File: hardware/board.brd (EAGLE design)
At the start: 53 x 30 mm, 45 parts, among them IC1 0915BM15A0001, J1 U.FL, U3 BLE113-A, X1 CTS_32X25_SMD, X3 MINI-USB-UX60-MB-5ST

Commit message: Update value of bias resistor
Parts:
- R3: value 58kOhm -> 56kOhm ± 1%
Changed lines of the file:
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@@
 <layer number="27" name="tValues" color="7" fill="1" visible="no" active="yes"/>
 <layer number="28" name="bValues" color="7" fill="1" visible="no" active="yes"/>
-<layer number="29" name="tStop" color="7" fill="3" visible="no" active="yes"/>
+<layer number="29" name="tStop" color="7" fill="3" visible="yes" active="yes"/>
 <layer number="30" name="bStop" color="7" fill="6" visible="no" active="yes"/>
 <layer number="31" name="tCream" color="7" fill="4" visible="no" active="yes"/>
@@
 <attribute name="VALUE" x="3.175" y="21.205" size="1.27" layer="27" rot="R180"/>
 </element>
-<element name="R3" library="rcl" package="R0402" value="58kOhm" x="21.3" y="3.5" smashed="yes" rot="R90">
+<element name="R3" library="rcl" package="R0402" value="56kOhm ± 1%" x="21.3" y="3.5" smashed="yes" rot="R90">
 <attribute name="VALUE" x="23.205" y="2.865" size="1.27" layer="27" rot="R90"/>
 </element>

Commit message: Update crystal value and part number
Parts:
- X1: value CTS_32X25_SMD -> 26MHz 10pF 10ppm -20C +70C
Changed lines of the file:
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@@
 <attribute name="VALUE" x="38.57" y="12.825" size="1.016" layer="27" rot="SR0"/>
 </element>
-<element name="X1" library="cts_crystal" package="CTS_32X25" value="CTS_32X25_SMD" x="17.985" y="14.645" smashed="yes">
+<element name="X1" library="cts_crystal" package="CTS_32X25" value="26MHz 10pF 10ppm -20C +70C" x="17.985" y="14.645" smashed="yes">
 <attribute name="VALUE" x="16.285" y="12.545" size="0.75" layer="27"/>
 </element>

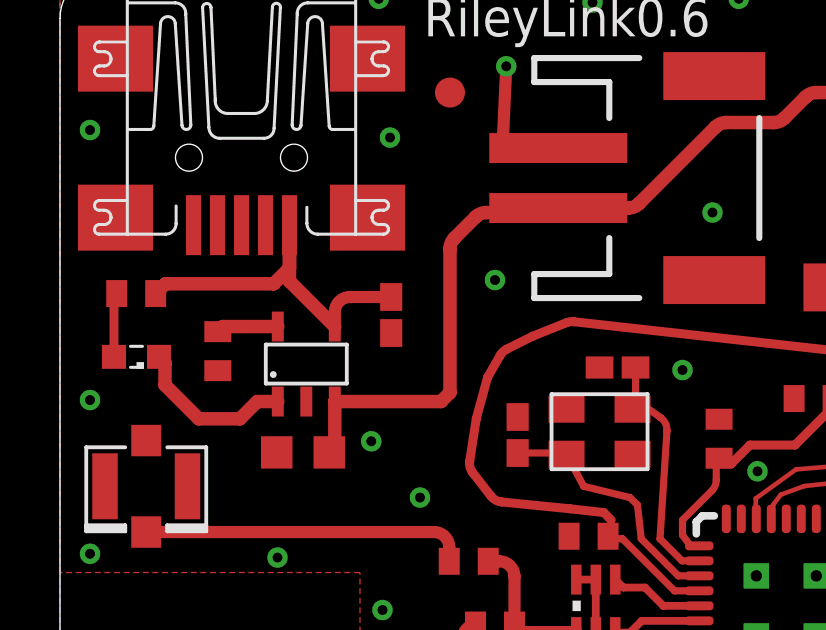
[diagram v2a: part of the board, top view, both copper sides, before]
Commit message: Add colors to leds, and switch 4.7uF cap from 0402 to 0603 package
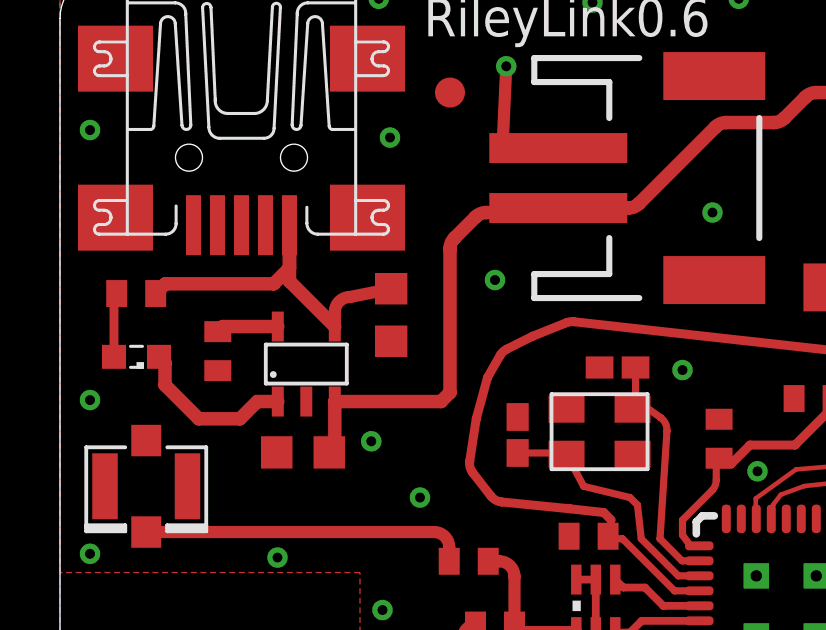
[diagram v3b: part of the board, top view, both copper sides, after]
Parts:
- C2: device rcl:C0402K -> rcl:C0603K
- LED1: value (none) -> red
- LED2, LED5: value (none) -> blue
- LED3, LED4: value (none) -> green
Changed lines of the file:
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@@
 <attribute name="VALUE" x="18.255" y="13.115" size="1.27" layer="27" rot="R180"/>
 </element>
-<element name="C2" library="rcl" package="C0402K" value="4.7uF" x="11.04" y="18.585" smashed="yes" rot="R270">
+<element name="C2" library="rcl" package="C0603K" value="4.7uF" x="11.04" y="18.585" smashed="yes" rot="R270">
 <attribute name="VALUE" x="9.59" y="19.085" size="1.016" layer="27" rot="R270"/>
 </element>
@@
 <attribute name="VALUE" x="26.9524" y="16.8466" size="2.0828" layer="27" ratio="10" rot="SR0"/>
 </element>
-<element name="LED1" library="led" package="SML0603" value="" x="2.55" y="17.19" smashed="yes" rot="R180">
+<element name="LED1" library="led" package="SML0603" value="red" x="2.55" y="17.19" smashed="yes" rot="R180">
 <attribute name="VALUE" x="3.55" y="19.19" size="1.27" layer="27" rot="R180"/>
 </element>
-<element name="LED2" library="led" package="SML0603" value="" x="51.65" y="19.05" smashed="yes" rot="R90">
+<element name="LED2" library="led" package="SML0603" value="blue" x="51.65" y="19.05" smashed="yes" rot="R90">
 <attribute name="VALUE" x="53.65" y="18.05" size="1.27" layer="27" rot="R90"/>
 </element>
-<element name="LED3" library="led" package="SML0603" value="" x="51.65" y="22.51" smashed="yes" rot="R90">
+<element name="LED3" library="led" package="SML0603" value="green" x="51.65" y="22.51" smashed="yes" rot="R90">
 <attribute name="VALUE" x="53.65" y="21.51" size="1.27" layer="27" rot="R90"/>
 </element>
-<element name="LED4" library="led" package="SML0603" value="" x="35.25" y="13.25" smashed="yes" rot="R270">
+<element name="LED4" library="led" package="SML0603" value="green" x="35.25" y="13.25" smashed="yes" rot="R270">
 <attribute name="VALUE" x="33.25" y="14.25" size="1.27" layer="27" rot="R270"/>
 </element>
-<element name="LED5" library="led" package="SML0603" value="" x="33.75" y="13.25" smashed="yes" rot="R270">
+<element name="LED5" library="led" package="SML0603" value="blue" x="33.75" y="13.25" smashed="yes" rot="R270">
 <attribute name="VALUE" x="31.75" y="14.25" size="1.27" layer="27" rot="R270"/>
 </element>
@@
 <wire x1="7.125" y1="19.625" x2="3.515" y2="19.625" width="0.45" layer="1"/>
 <wire x1="3.515" y1="19.625" x2="3.19" y2="19.3" width="0.45" layer="1"/>
-<wire x1="11.04" y1="19.185" x2="9.668" y2="19.185" width="0.4064" layer="1"/>
+<wire x1="11.04" y1="19.46" x2="9.668" y2="19.185" width="0.4064" layer="1"/>
 <wire x1="9.668" y1="19.185" x2="9.16" y2="18.677" width="0.4064" layer="1" curve="90"/>
 <wire x1="9.16" y1="18.677" x2="9.16" y2="18.2" width="0.4064" layer="1"/>

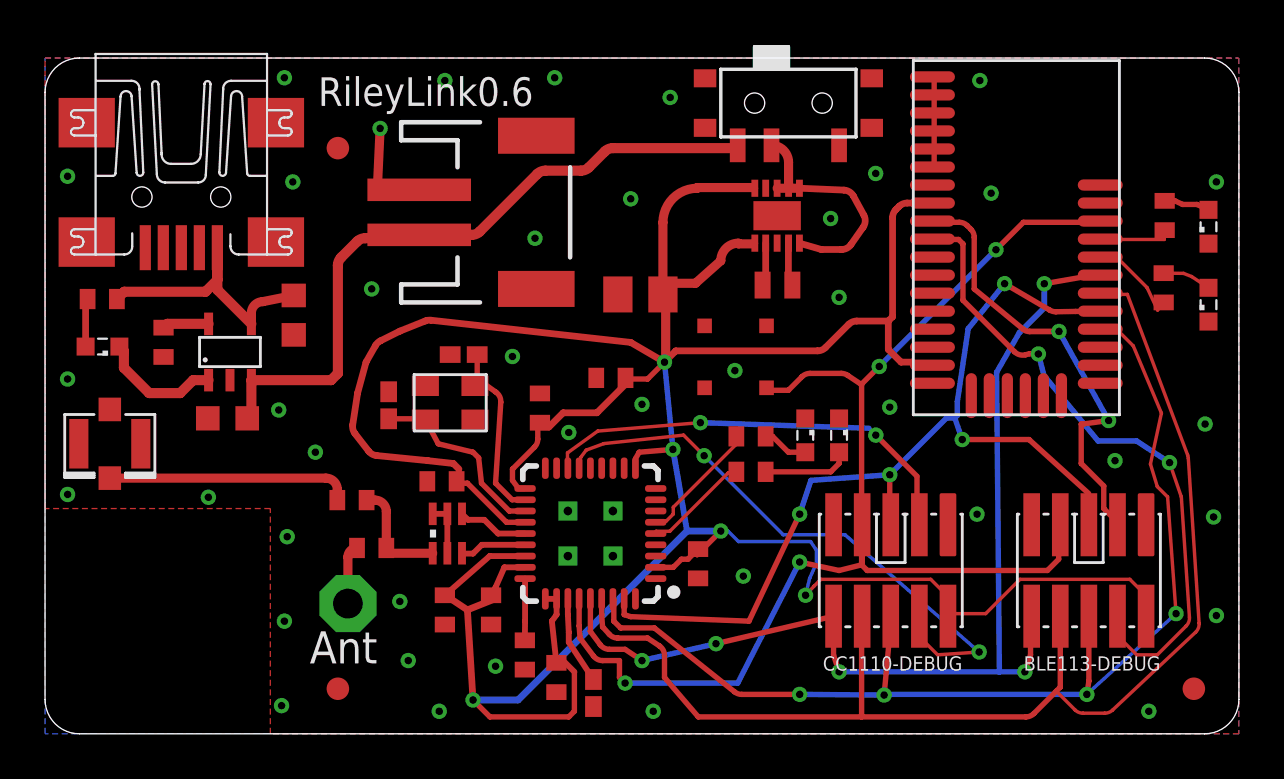
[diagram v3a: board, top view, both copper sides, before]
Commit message: Update C11 to 0805
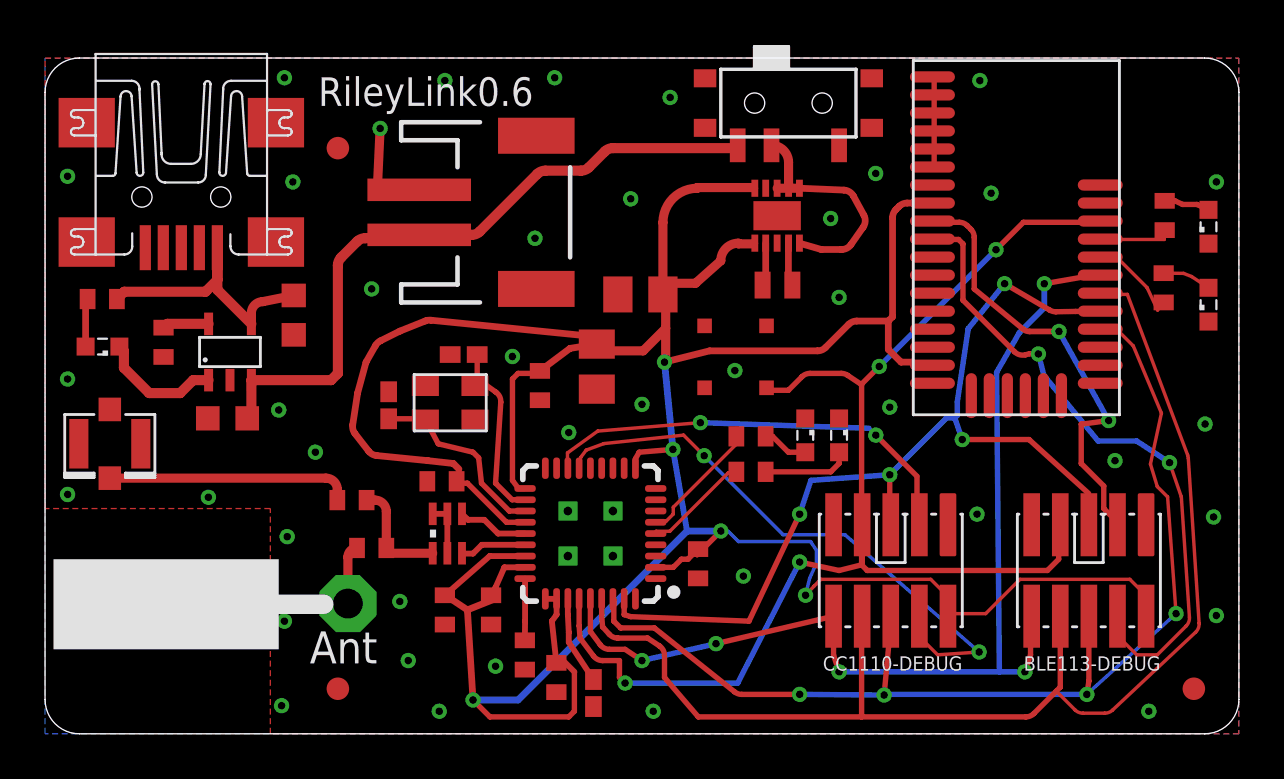
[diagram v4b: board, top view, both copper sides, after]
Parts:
- C11: device rcl:C0402 -> rcl:C0805K
- moved C12 1.00 mm to (22.0, 15.5), turned to 270 degrees
- moved C11 0.80 mm to (24.5, 16.3), turned to 270 degrees
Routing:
- net VDD: track 152.6 -> 151.7 mm
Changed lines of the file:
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@@
 <layer number="27" name="tValues" color="7" fill="1" visible="no" active="yes"/>
 <layer number="28" name="bValues" color="7" fill="1" visible="no" active="yes"/>
-<layer number="29" name="tStop" color="7" fill="3" visible="yes" active="yes"/>
+<layer number="29" name="tStop" color="7" fill="3" visible="no" active="yes"/>
 <layer number="30" name="bStop" color="7" fill="6" visible="no" active="yes"/>
 <layer number="31" name="tCream" color="7" fill="4" visible="no" active="yes"/>
@@
 <text x="12.125" y="27.875" size="1.27" layer="25">RileyLink0.6</text>
 <text x="11.75" y="3.125" size="1.4224" layer="25">Ant</text>
+<wire x1="12.375" y1="5.75" x2="10.375" y2="5.75" width="0.8636" layer="112"/>
+<rectangle x1="0.375" y1="3.75" x2="10.375" y2="7.75" layer="112"/>
 </plain>
 <attributes>
@@
 <attribute name="VALUE" x="17.895" y="6.135" size="1.27" layer="27" rot="R270"/>
 </element>
-<element name="C11" library="rcl" package="C0402" value="100uF" x="25.12" y="15.8" smashed="yes" rot="R180">
-<attribute name="VALUE" x="25.755" y="17.705" size="1.27" layer="27" rot="R180"/>
-</element>
-<element name="C12" library="rcl" package="C0402" value="100nF" x="21.97" y="14.46" smashed="yes" rot="R90">
-<attribute name="VALUE" x="23.875" y="13.825" size="1.27" layer="27" rot="R90"/>
+<element name="C11" library="rcl" package="C0805K" value="100uF" x="24.495" y="16.3" smashed="yes" rot="R270">
+<attribute name="VALUE" x="22.59" y="16.935" size="1.27" layer="27" rot="R270"/>
+</element>
+<element name="C12" library="rcl" package="C0402" value="100nF" x="21.97" y="15.46" smashed="yes" rot="R270">
+<attribute name="VALUE" x="20.065" y="16.095" size="1.27" layer="27" rot="R270"/>
 </element>
 <element name="C13" library="rcl" package="C0402" value="100nF" x="17.62" y="11.21" smashed="yes" rot="R180">
@@
 <wire x1="19.75" y1="0.75" x2="19" y2="1.5" width="0.24" layer="1"/>
 <via x="27.5" y="16.5" extent="1-16" drill="0.3302"/>
-<wire x1="27.5" y1="16.5" x2="27.875" y2="12.625" width="0.24" layer="16"/>
-<wire x1="27.5" y1="16.5" x2="26.75" y2="15.75" width="0.24" layer="1"/>
-<wire x1="26.75" y1="15.75" x2="25.7556" y2="15.75" width="0.24" layer="1"/>
+<wire x1="27.5" y1="16.5" x2="27.875" y2="12.625" width="0.3" layer="16"/>
 <via x="27.875" y="12.625" extent="1-16" drill="0.3302"/>
-<wire x1="25.7556" y1="15.75" x2="25.75" y2="15.75" width="0.24" layer="1"/>
 <wire x1="26.21" y1="11.79" x2="26.21" y2="12.21" width="0.24" layer="1"/>
 <wire x1="26.21" y1="12.21" x2="26.375" y2="12.5" width="0.24" layer="1"/>
@@
 <wire x1="38.5572" y1="16.4592" x2="39.3192" y2="16.4592" width="0.1524" layer="1"/>
 <wire x1="39.3192" y1="16.4592" x2="39.395" y2="16.3625" width="0.1524" layer="1"/>
-<wire x1="25.7556" y1="15.8496" x2="25.77" y2="15.8" width="0.1524" layer="1"/>
-<wire x1="25.7556" y1="15.8496" x2="25.7556" y2="15.75" width="0.1524" layer="1"/>
 <wire x1="40.0812" y1="6.096" x2="40.0812" y2="5.334" width="0.1524" layer="1"/>
 <wire x1="39.3192" y1="6.858" x2="40.0812" y2="6.096" width="0.1524" layer="1"/>
@@
 <wire x1="21.31" y1="10.89" x2="21.015" y2="10.89" width="0.24" layer="1"/>
 <wire x1="21.015" y1="10.89" x2="20.75" y2="11.25" width="0.24" layer="1"/>
-<wire x1="20.75" y1="11.25" x2="20.75" y2="11.75" width="0.24" layer="1"/>
-<wire x1="20.75" y1="11.75" x2="21.726209375" y2="12.726209375" width="0.24" layer="1"/>
-<wire x1="21.726209375" y1="12.726209375" x2="21.875" y2="13.085421875" width="0.24" layer="1" curve="45.000352"/>
-<wire x1="21.875" y1="13.085421875" x2="21.875" y2="13.625" width="0.24" layer="1"/>
-<wire x1="21.875" y1="13.625" x2="21.875" y2="13.715" width="0.24" layer="1"/>
-<wire x1="21.875" y1="13.715" x2="21.97" y2="13.81" width="0.24" layer="1"/>
 <wire x1="21.31" y1="9.39" x2="20.485" y2="9.39" width="0.24" layer="1"/>
 <wire x1="20.485" y1="9.39" x2="18.75" y2="11.125" width="0.24" layer="1"/>
@@
 <wire x1="15.75" y1="17.875" x2="16.88178125" y2="18.3277125" width="0.3" layer="1"/>
 <wire x1="16.88178125" y1="18.3277125" x2="17.126546875" y2="18.360940625" width="0.3" layer="1" curve="-28.141614"/>
-<wire x1="17.126546875" y1="18.360940625" x2="26" y2="17.375" width="0.3" layer="1"/>
 <wire x1="18.355" y1="11.125" x2="18.355" y2="11.23" width="0.24" layer="1"/>
 <wire x1="18.355" y1="11.23" x2="18.375" y2="11.25" width="0.24" layer="1"/>
-<wire x1="28" y1="17" x2="27.5" y2="16.5" width="0.3" layer="1"/>
 <wire x1="37.4356" y1="18.324" x2="36.034421875" y2="18.324" width="0.3" layer="1"/>
 <wire x1="36.034421875" y1="18.324" x2="35.675209375" y2="18.175209375" width="0.3" layer="1" curve="45.000249"/>
 <wire x1="35.675209375" y1="18.175209375" x2="34.648790625" y2="17.148790625" width="0.3" layer="1"/>
 <wire x1="34.648790625" y1="17.148790625" x2="34.289578125" y2="17" width="0.3" layer="1" curve="-45.000352"/>
-<wire x1="34.289578125" y1="17" x2="28" y2="17" width="0.3" layer="1"/>
+<wire x1="34.289578125" y1="17" x2="29.5" y2="17" width="0.3" layer="1"/>
 <wire x1="37.4356" y1="18.324" x2="37.4356" y2="17.0644" width="0.3" layer="1"/>
 <wire x1="37.4356" y1="17.0644" x2="38" y2="16.5" width="0.3" layer="1"/>
@@
 <wire x1="37.625" y1="22.914578125" x2="37.625" y2="18.5134" width="0.3" layer="1"/>
 <wire x1="37.625" y1="18.5134" x2="37.4356" y2="18.324" width="0.3" layer="1"/>
-<wire x1="26" y1="17.375" x2="27.5" y2="16.5" width="0.3" layer="1"/>
-<wire x1="21.875" y1="13.625" x2="22.375" y2="13.625" width="0.3" layer="1"/>
-<wire x1="22.375" y1="13.625" x2="23" y2="14.25" width="0.3" layer="1"/>
-<wire x1="23" y1="14.25" x2="24.5" y2="14.25" width="0.3" layer="1"/>
-<wire x1="24.5" y1="14.25" x2="25.875" y2="15.625" width="0.3" layer="1"/>
-<wire x1="25.7556" y1="15.75" x2="25.7556" y2="15.7444" width="0.3" layer="1"/>
-<wire x1="25.7556" y1="15.7444" x2="25.875" y2="15.625" width="0.3" layer="1"/>
 <wire x1="28.954" y1="24.2192" x2="27.43" y2="22.6952" width="0.4064" layer="1" curve="90"/>
 <wire x1="27.43" y1="22.6952" x2="27.43" y2="19.505" width="0.4064" layer="1"/>
@@
 <wire x1="27.925" y1="20" x2="27.43" y2="19.505" width="0.4064" layer="1" curve="90"/>
 <wire x1="27.43" y1="19.505" x2="27.552578125" y2="19.382421875" width="0.4064" layer="1" curve="-90"/>
-<wire x1="27.552578125" y1="19.382421875" x2="27.552578125" y2="16.4567" width="0.4064" layer="1"/>
+<wire x1="27.552578125" y1="19.382421875" x2="27.552578125" y2="18" width="0.4064" layer="1"/>
+<wire x1="27.552578125" y1="18" x2="27.552578125" y2="16.4567" width="0.4064" layer="1"/>
 <wire x1="31.5094" y1="24.2192" x2="31.375" y2="24.2192" width="0.3048" layer="1"/>
 <wire x1="31.375" y1="24.2192" x2="31.375" y2="24.25" width="0.3048" layer="1"/>
@@
 <wire x1="31.375" y1="21.75" x2="30.7808" y2="21.75" width="0.4064" layer="1"/>
 <wire x1="30.7808" y1="21.75" x2="30.7808" y2="21.7808" width="0.4064" layer="1"/>
-<wire x1="27.5" y1="16.5" x2="27.552578125" y2="16.4567" width="0" layer="19" extent="1-1"/>
+<wire x1="20.75" y1="11.25" x2="20.75" y2="15.75" width="0.24" layer="1"/>
+<wire x1="20.75" y1="15.75" x2="21" y2="16" width="0.24" layer="1"/>
+<wire x1="21" y1="16" x2="21.86" y2="16" width="0.24" layer="1"/>
+<wire x1="21.97" y1="16.11" x2="23.305" y2="17.11" width="0.3" layer="1"/>
+<wire x1="23.305" y1="17.11" x2="24.495" y2="17.3" width="0.3" layer="1"/>
+<wire x1="24.795" y1="17" x2="24.495" y2="17.3" width="0.3" layer="1"/>
+<wire x1="24.4874875" y1="17.625" x2="17.126546875" y2="18.360940625" width="0.3" layer="1"/>
+<wire x1="24.495" y1="17.3" x2="24.495" y2="17.6174875" width="0.3" layer="1"/>
+<wire x1="24.495" y1="17.6174875" x2="24.4874875" y2="17.625" width="0.3" layer="1"/>
+<wire x1="29.5" y1="17" x2="27.5" y2="16.5" width="0.3" layer="1"/>
+<wire x1="27.552578125" y1="16.4567" x2="27.5433" y2="16.4567" width="0.3" layer="1"/>
+<wire x1="27.5433" y1="16.4567" x2="27.5" y2="16.5" width="0.3" layer="1"/>
+<wire x1="21.86" y1="16" x2="21.97" y2="16.11" width="0.3" layer="1"/>
+<wire x1="24.795" y1="17" x2="26.552578125" y2="17" width="0.4064" layer="1"/>
+<wire x1="26.552578125" y1="17" x2="27.552578125" y2="18" width="0.4064" layer="1"/>
 </signal>
 <signal name="N$3">
